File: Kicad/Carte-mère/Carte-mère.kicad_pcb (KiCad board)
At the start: 2 copper layers, 3 parts

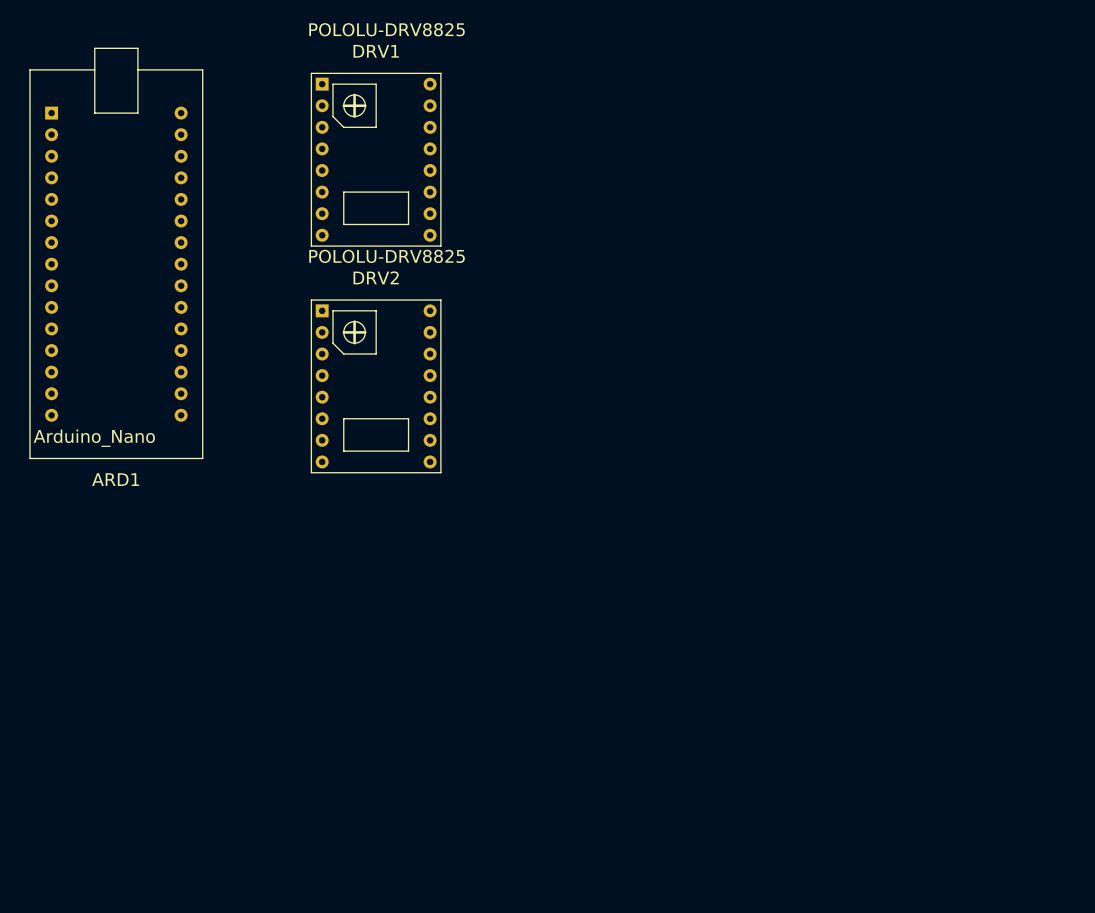
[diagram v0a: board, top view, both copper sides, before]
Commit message: Modification du circuit imprimée
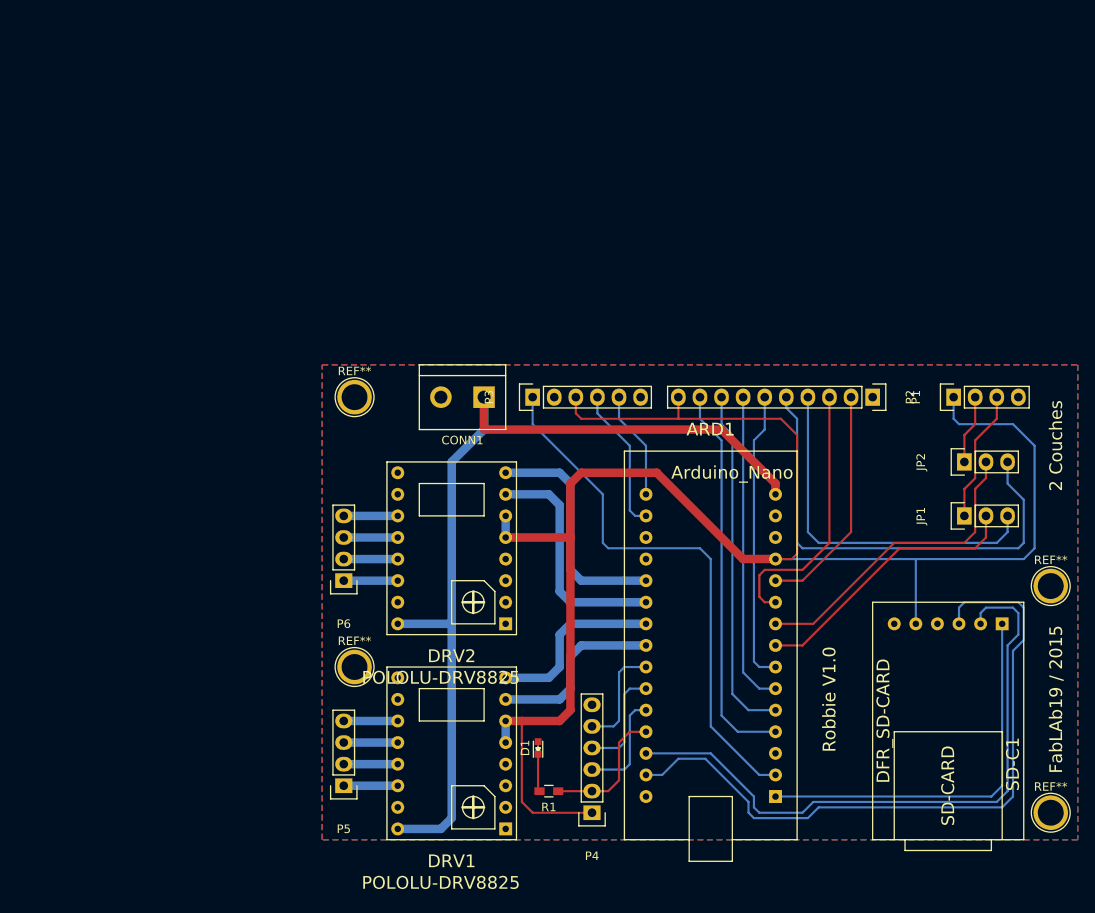
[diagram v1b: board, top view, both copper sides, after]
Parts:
- added CONN1: CONN_2, Connect:bornier2, F.Cu at (116.8, 86.4)
- added D1: LED, LEDs:LED-0603, F.Cu at (125.7, 127.6)
- added JP1: JUMPER3, Pin_Headers:Pin_Header_Straight_1x03, F.Cu at (175.9, 100.3)
- added JP2: JUMPER3, Pin_Headers:Pin_Header_Straight_1x03, F.Cu at (175.9, 94.0)
- added P1: CONN_01X10, Pin_Headers:Pin_Header_Straight_1x10, F.Cu at (165.1, 86.4)
- added P2: CONN_01X04, Pin_Headers:Pin_Header_Straight_1x04, F.Cu at (174.6, 86.4)
- added P3: CONN_01X06, Pin_Headers:Pin_Header_Straight_1x06, F.Cu at (125.1, 86.4)
- added P4: CONN_01X06, Pin_Headers:Pin_Header_Straight_1x06, F.Cu at (132.1, 135.3)
- added P5: CONN_01X04, Pin_Headers:Pin_Header_Straight_1x04, F.Cu at (102.9, 132.1)
- added P6: CONN_01X04, Pin_Headers:Pin_Header_Straight_1x04, F.Cu at (102.9, 108.0)
- added R1: 200, Resistors_SMD:R_0603_HandSoldering, F.Cu at (127.0, 132.7)
- added REF**: 1pin, Connect:1pin, F.Cu at (186.1, 135.3)
- added REF**: 1pin, Connect:1pin, F.Cu at (186.1, 108.6)
- added REF**: 1pin, Connect:1pin, F.Cu at (104.1, 86.4)
- added REF**: 1pin, Connect:1pin, F.Cu at (104.1, 118.1)
- added SD-C1: DFR_SD-CARD, DF-ROBOT_SD-CARD:DFR_SD-CARD, F.Cu at (172.7, 113.0)
- moved ARD1 85.9 mm to (146.1, 118.1), turned to 180 degrees
- moved DRV1 67.6 mm to (114.3, 127.0), turned to 180 degrees
- moved DRV2 17.7 mm to (114.3, 102.9), turned to 180 degrees
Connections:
- ARD1 pad 1: (no net) -> Net-(ARD1-Pad1)
- ARD1 pad 10: (no net) -> Net-(ARD1-Pad10)
- ARD1 pad 11: (no net) -> Net-(ARD1-Pad11)
- ARD1 pad 12: (no net) -> +5V
- ARD1 pad 14: (no net) -> GND
- ARD1 pad 15: (no net) -> +BATT
- ARD1 pad 16: (no net) -> Net-(ARD1-Pad16)
- ARD1 pad 17: (no net) -> Net-(ARD1-Pad17)
- ARD1 pad 2: (no net) -> +3.3V
- ARD1 pad 20: (no net) -> Net-(ARD1-Pad20)
- ARD1 pad 21: (no net) -> Net-(ARD1-Pad21)
- ARD1 pad 22: (no net) -> Net-(ARD1-Pad22)
- ARD1 pad 23: (no net) -> Net-(ARD1-Pad23)
- ARD1 pad 24: (no net) -> Net-(ARD1-Pad24)
- ARD1 pad 25: (no net) -> Net-(ARD1-Pad25)
- ARD1 pad 26: (no net) -> Net-(ARD1-Pad26)
- ARD1 pad 27: (no net) -> Net-(ARD1-Pad27)
- ARD1 pad 28: (no net) -> Net-(ARD1-Pad28)
- ARD1 pad 29: (no net) -> Net-(ARD1-Pad29)
- ARD1 pad 4: (no net) -> Net-(ARD1-Pad4)
- ARD1 pad 5: (no net) -> Net-(ARD1-Pad5)
- ARD1 pad 6: (no net) -> Net-(ARD1-Pad6)
- ARD1 pad 7: (no net) -> Net-(ARD1-Pad7)
- ARD1 pad 8: (no net) -> Net-(ARD1-Pad8)
- ARD1 pad 9: (no net) -> Net-(ARD1-Pad9)
- DRV1 pad 11: (no net) -> Net-(DRV1-Pad11)
- DRV1 pad 12: (no net) -> Net-(DRV1-Pad12)
- DRV1 pad 13: (no net) -> Net-(DRV1-Pad13)
- DRV1 pad 14: (no net) -> Net-(DRV1-Pad14)
- DRV1 pad 16: (no net) -> +BATT
- DRV1 pad 5: (no net) -> +5V
- DRV1 pad 6: (no net) -> +5V
- DRV1 pad 7: (no net) -> Net-(ARD1-Pad23)
- DRV1 pad 8: (no net) -> Net-(ARD1-Pad22)
- DRV1 pad 9: (no net) -> GND
- DRV2 pad 11: (no net) -> Net-(DRV2-Pad11)
- DRV2 pad 12: (no net) -> Net-(DRV2-Pad12)
- DRV2 pad 13: (no net) -> Net-(DRV2-Pad13)
- DRV2 pad 14: (no net) -> Net-(DRV2-Pad14)
- DRV2 pad 16: (no net) -> +BATT
- DRV2 pad 5: (no net) -> +5V
- DRV2 pad 6: (no net) -> +5V
- DRV2 pad 7: (no net) -> Net-(ARD1-Pad21)
- DRV2 pad 8: (no net) -> Net-(ARD1-Pad20)
- DRV2 pad 9: (no net) -> GND
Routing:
- net +5V: track 0.00 -> 207.1 mm
- net +BATT: track 0.00 -> 106.3 mm
- net Net-(ARD1-Pad29): track 0.00 -> 81.5 mm
- net Net-(ARD1-Pad28): track 0.00 -> 75.0 mm
- net +3.3V: track 0.00 -> 63.7 mm
- net Net-(JP2-Pad3): track 0.00 -> 55.2 mm
- net Net-(ARD1-Pad1): track 0.00 -> 46.2 mm
- net Net-(ARD1-Pad4): track 0.00 -> 45.7 mm
- net Net-(JP1-Pad3): track 0.00 -> 42.3 mm
- net Net-(ARD1-Pad5): track 0.00 -> 41.3 mm
- net Net-(ARD1-Pad6): track 0.00 -> 37.0 mm
- net Net-(ARD1-Pad9): track 0.00 -> 36.7 mm
- net Net-(ARD1-Pad7): track 0.00 -> 35.7 mm
- net Net-(ARD1-Pad8): track 0.00 -> 32.6 mm
- net Net-(ARD1-Pad10): track 0.00 -> 31.7 mm
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- added copper zone on B.Cu, net GND
- added copper zone on F.Cu, net GND
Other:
- net class 1mm added: clearance 0.254, trace_width 1, via_dia 1.635, via_drill 1
- net class 2mm added: clearance 0.254, trace_width 2, via_dia 2.635, via_drill 2
- rule pad_to_mask_clearance: 0 -> 0.2
- board text added: "2 Couches"
- board text added: "FabLAb19 / 2015"
- board text added: "Robbie V1.0"

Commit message: Mise à jour de la carte mère
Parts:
- removed the REF** at (186.1, 135.3)
- removed the REF** at (186.1, 108.6)
- removed the REF** at (104.1, 118.1)
- added REF**: 1pin, Connect:1pin, F.Cu at (104.1, 116.8)
- added REF**: 1pin, Connect:1pin, F.Cu at (185.4, 134.6)
- added REF**: 1pin, Connect:1pin, F.Cu at (185.4, 109.2)
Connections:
- ARD1 pad 19: (no net) -> GND
- DRV1 pad 15: (no net) -> GND
- DRV2 pad 15: (no net) -> GND
- REF** pad 1: (no net) -> GND
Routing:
- net +5V: track 207.1 -> 205.6 mm
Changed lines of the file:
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@@
 (kicad_pcb (version 4) (host pcbnew "(2014-jul-16 BZR unknown)-product")
   (general
-    (links 57)
-    (no_connects 1)
+    (links 62)
+    (no_connects 0)
     (area 0 0 0 0)
     (thickness 1.6)
     (drawings 7)
-    (tracks 211)
+    (tracks 213)
     (zones 0)
     (modules 19)
@@
     (mod_text_size 1.5 1.5)
     (mod_text_width 0.15)
-    (pad_size 1.524 1.524)
-    (pad_drill 0.762)
+    (pad_size 4.064 4.064)
+    (pad_drill 3.048)
     (pad_to_mask_clearance 0.2)
     (aux_axis_origin 0 0)
@@
       (net 15 "Net-(ARD1-Pad17)"))
     (pad 18 thru_hole circle (at 7.62 15.24 180) (size 1.524 1.524) (drill 0.762) (layers *.Cu *.Mask F.SilkS))
-    (pad 19 thru_hole circle (at 7.62 12.7 180) (size 1.524 1.524) (drill 0.762) (layers *.Cu *.Mask F.SilkS))
+    (pad 19 thru_hole circle (at 7.62 12.7 180) (size 1.524 1.524) (drill 0.762) (layers *.Cu *.Mask F.SilkS)
+      (net 12 GND))
     (pad 20 thru_hole circle (at 7.62 10.16 180) (size 1.524 1.524) (drill 0.762) (layers *.Cu *.Mask F.SilkS)
       (net 16 "Net-(ARD1-Pad20)"))
@@
     (pad 14 thru_hole circle (at 5.08 -5.08 180) (size 1.524 1.524) (drill 0.762) (layers *.Cu *.Mask F.SilkS)
       (net 30 "Net-(DRV1-Pad14)"))
-    (pad 15 thru_hole circle (at 5.08 -7.62 180) (size 1.524 1.524) (drill 0.762) (layers *.Cu *.Mask F.SilkS))
+    (pad 15 thru_hole circle (at 5.08 -7.62 180) (size 1.524 1.524) (drill 0.762) (layers *.Cu *.Mask F.SilkS)
+      (net 12 GND))
     (pad 16 thru_hole circle (at 5.08 -10.16 180) (size 1.524 1.524) (drill 0.762) (layers *.Cu *.Mask F.SilkS)
       (net 13 +BATT))
@@
     (pad 14 thru_hole circle (at 5.08 -5.08 180) (size 1.524 1.524) (drill 0.762) (layers *.Cu *.Mask F.SilkS)
       (net 34 "Net-(DRV2-Pad14)"))
-    (pad 15 thru_hole circle (at 5.08 -7.62 180) (size 1.524 1.524) (drill 0.762) (layers *.Cu *.Mask F.SilkS))
+    (pad 15 thru_hole circle (at 5.08 -7.62 180) (size 1.524 1.524) (drill 0.762) (layers *.Cu *.Mask F.SilkS)
+      (net 12 GND))
     (pad 16 thru_hole circle (at 5.08 -10.16 180) (size 1.524 1.524) (drill 0.762) (layers *.Cu *.Mask F.SilkS)
       (net 13 +BATT))
@@
   )
   (module Connect:1pin (layer F.Cu)
-    (at 186.055 135.255)
-    (descr "module 1 pin (ou trou mecanique de percage)")
-    (tags DEV)
-    (fp_text reference REF** (at 0 -3.048) (layer F.SilkS)
-      (effects (font (size 1 1) (thickness 0.15)))
-    )
-    (fp_text value 1pin (at 0 2.794) (layer F.Fab)
-      (effects (font (size 1 1) (thickness 0.15)))
-    )
-    (fp_circle (center 0 0) (end 0 -2.286) (layer F.SilkS) (width 0.15))
-    (pad 1 thru_hole circle (at 0 0) (size 4.064 4.064) (drill 3.048) (layers *.Cu *.Mask F.SilkS))
-  )
-  (module Connect:1pin (layer F.Cu)
-    (at 186.055 108.585)
-    (descr "module 1 pin (ou trou mecanique de percage)")
-    (tags DEV)
-    (fp_text reference REF** (at 0 -3.048) (layer F.SilkS)
-      (effects (font (size 1 1) (thickness 0.15)))
-    )
-    (fp_text value 1pin (at 0 2.794) (layer F.Fab)
-      (effects (font (size 1 1) (thickness 0.15)))
-    )
-    (fp_circle (center 0 0) (end 0 -2.286) (layer F.SilkS) (width 0.15))
-    (pad 1 thru_hole circle (at 0 0) (size 4.064 4.064) (drill 3.048) (layers *.Cu *.Mask F.SilkS))
-  )
-  (module Connect:1pin (layer F.Cu)
     (at 104.14 86.36)
     (descr "module 1 pin (ou trou mecanique de percage)")
@@
     )
     (fp_circle (center 0 0) (end 0 -2.286) (layer F.SilkS) (width 0.15))
-    (pad 1 thru_hole circle (at 0 0) (size 4.064 4.064) (drill 3.048) (layers *.Cu *.Mask F.SilkS))
+    (pad 1 thru_hole circle (at 0 0) (size 4.064 4.064) (drill 3.048) (layers *.Cu *.Mask F.SilkS)
+      (net 12 GND))
   )
   (module Connect:1pin (layer F.Cu)
-    (at 104.14 118.11)
+    (at 104.14 116.84)
     (descr "module 1 pin (ou trou mecanique de percage)")
     (tags DEV)
@@
     )
     (fp_circle (center 0 0) (end 0 -2.286) (layer F.SilkS) (width 0.15))
-    (pad 1 thru_hole circle (at 0 0) (size 4.064 4.064) (drill 3.048) (layers *.Cu *.Mask F.SilkS))
+    (pad GND thru_hole circle (at 0 0) (size 4.064 4.064) (drill 3.048) (layers *.Cu *.Mask F.SilkS))
+  )
+  (module Connect:1pin (layer F.Cu)
+    (at 185.42 134.62)
+    (descr "module 1 pin (ou trou mecanique de percage)")
+    (tags DEV)
+    (fp_text reference REF** (at 0 -3.048) (layer F.SilkS)
+      (effects (font (size 1 1) (thickness 0.15)))
+    )
+    (fp_text value 1pin (at 0 2.794) (layer F.Fab)
+      (effects (font (size 1 1) (thickness 0.15)))
+    )
+    (fp_circle (center 0 0) (end 0 -2.286) (layer F.SilkS) (width 0.15))
+    (pad GND thru_hole circle (at 0 0) (size 4.064 4.064) (drill 3.048) (layers *.Cu *.Mask F.SilkS))
+  )
+  (module Connect:1pin (layer F.Cu)
+    (at 185.42 109.22)
+    (descr "module 1 pin (ou trou mecanique de percage)")
+    (tags DEV)
+    (fp_text reference REF** (at 0 -3.048) (layer F.SilkS)
+      (effects (font (size 1 1) (thickness 0.15)))
+    )
+    (fp_text value 1pin (at 0 2.794) (layer F.Fab)
+      (effects (font (size 1 1) (thickness 0.15)))
+    )
+    (fp_circle (center 0 0) (end 0 -2.286) (layer F.SilkS) (width 0.15))
+    (pad 1 thru_hole circle (at 0 0) (size 4.064 4.064) (drill 3.048) (layers *.Cu *.Mask F.SilkS)
+      (net 12 GND))
   )
   (gr_text "2 Couches" (at 186.69 92.075 90) (layer F.SilkS)
@@
   (segment (start 179.07 133.35) (end 153.67 133.35) (width 0.254) (layer B.Cu) (net 1))
   (segment (start 180.34 132.08) (end 179.07 133.35) (width 0.254) (layer B.Cu) (net 1))
-  (segment (start 125.095 86.36) (end 125.095 89.535) (width 0.254) (layer B.Cu) (net 2))
+  (segment (start 125.095 86.36) (end 125.095 88.9) (width 0.254) (layer B.Cu) (net 2) (status 400000))
   (segment (start 151.765 130.81) (end 153.67 130.81) (width 0.254) (layer B.Cu) (net 2))
   (segment (start 146.05 125.095) (end 151.765 130.81) (width 0.254) (layer B.Cu) (net 2))
@@
   (segment (start 133.985 104.14) (end 144.78 104.14) (width 0.254) (layer B.Cu) (net 2))
   (segment (start 133.35 103.505) (end 133.985 104.14) (width 0.254) (layer B.Cu) (net 2))
-  (segment (start 133.35 97.79) (end 133.35 103.505) (width 0.254) (layer B.Cu) (net 2))
-  (segment (start 125.095 89.535) (end 133.35 97.79) (width 0.254) (layer B.Cu) (net 2))
+  (segment (start 133.35 97.155) (end 133.35 103.505) (width 0.254) (layer B.Cu) (net 2))
+  (segment (start 125.095 88.9) (end 133.35 97.155) (width 0.254) (layer B.Cu) (net 2))
   (segment (start 144.78 86.36) (end 144.78 88.9) (width 0.254) (layer B.Cu) (net 3))
   (segment (start 149.225 125.73) (end 153.67 125.73) (width 0.254) (layer B.Cu) (net 3))
@@
   (segment (start 125.095 135.255) (end 132.08 135.255) (width 0.254) (layer F.Cu) (net 11))
   (segment (start 123.825 133.985) (end 125.095 135.255) (width 0.254) (layer F.Cu) (net 11))
-  (segment (start 129.54 102.87) (end 129.54 123.19) (width 1) (layer F.Cu) (net 11))
-  (segment (start 128.27 124.46) (end 123.825 124.46) (width 1) (layer F.Cu) (net 11))
   (segment (start 123.825 124.46) (end 121.92 124.46) (width 1) (layer F.Cu) (net 11))
-  (segment (start 129.54 123.19) (end 128.27 124.46) (width 1) (layer F.Cu) (net 11))
   (segment (start 121.92 102.87) (end 129.54 102.87) (width 1) (layer F.Cu) (net 11))
+  (segment (start 130.81 95.25) (end 139.7 95.25) (width 1) (layer F.Cu) (net 11))
+  (segment (start 129.54 96.52) (end 130.81 95.25) (width 1) (layer F.Cu) (net 11))
+  (segment (start 129.54 102.87) (end 129.54 96.52) (width 1) (layer F.Cu) (net 11))
   (segment (start 149.86 105.41) (end 153.67 105.41) (width 1) (layer F.Cu) (net 11))
-  (segment (start 129.54 102.87) (end 129.54 96.52) (width 1) (layer F.Cu) (net 11))
-  (segment (start 129.54 96.52) (end 130.81 95.25) (width 1) (layer F.Cu) (net 11))
-  (segment (start 130.81 95.25) (end 139.7 95.25) (width 1) (layer F.Cu) (net 11))
   (segment (start 139.7 95.25) (end 149.86 105.41) (width 1) (layer F.Cu) (net 11))
   (segment (start 121.92 124.46) (end 121.92 127) (width 1) (layer B.Cu) (net 11))
   (segment (start 121.92 100.33) (end 121.92 102.87) (width 1) (layer B.Cu) (net 11))
+  (segment (start 125.73 124.46) (end 127 123.19) (width 1) (layer F.Cu) (net 11))
+  (segment (start 127 123.19) (end 127 108.585) (width 1) (layer F.Cu) (net 11))
+  (segment (start 127 108.585) (end 129.54 106.045) (width 1) (layer F.Cu) (net 11))
+  (segment (start 129.54 106.045) (end 129.54 102.87) (width 1) (layer F.Cu) (net 11))
+  (segment (start 123.825 124.46) (end 125.73 124.46) (width 1) (layer F.Cu) (net 11))
   (segment (start 119.38 86.36) (end 119.38 90.17) (width 1) (layer F.Cu) (net 13))
   (segment (start 153.67 96.52) (end 153.67 97.79) (width 1) (layer F.Cu) (net 13))

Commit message: Modification PCB pour prendre en compte les remarques faites à l'IUT
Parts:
- removed the REF** at (104.1, 86.4)
- removed the REF** at (104.1, 116.8)
- removed the REF** at (185.4, 134.6)
- removed the REF** at (185.4, 109.2)
- added BPN1: Bouton_poussoir_CI, Boutons:BPN-CI, F.Cu at (189.9, 128.3)
- added P7: CONN_01X02, Pin_Headers:Pin_Header_Straight_1x02, F.Cu at (168.3, 96.5)
- added REF**: 1pin, Connect:1pin, F.Cu at (191.1, 147.3)
- added REF**: 1pin, Connect:1pin, F.Cu at (109.9, 147.3)
- added REF**: 1pin, Connect:1pin, F.Cu at (109.9, 68.6)
- added REF**: 1pin, Connect:1pin, F.Cu at (191.1, 68.6)
- moved R1 69.5 mm to (191.1, 106.0), turned to 270 degrees
- moved D1 67.3 mm to (191.1, 111.8), turned to 270 degrees
- moved P4 45.3 mm to (155.6, 96.5), turned to 270 degrees
- moved P3 33.0 mm to (155.6, 73.7), turned to 270 degrees
- moved P1 22.4 mm to (183.5, 73.7)
- moved JP2 18.0 mm to (173.4, 111.8), turned to 180 degrees
- moved DRV1 14.8 mm to (125.1, 137.2)
- moved ARD1 14.7 mm to (150.5, 132.1)
- moved DRV2 14.0 mm to (125.1, 111.8)
- moved SD-C1 14.0 mm to (173.4, 127.0)
- moved P2 13.5 mm to (183.5, 96.5), turned to 270 degrees
- moved JP1 11.7 mm to (178.4, 111.8), turned to 180 degrees
- moved P5 10.8 mm to (112.4, 137.2)
- moved P6 10.3 mm to (112.4, 111.8)
- moved CONN1 3.18 mm to (114.9, 88.9), turned to 270 degrees
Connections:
- ARD1 pad 13: (no net) -> Net-(ARD1-Pad13)
- ARD1 pad 18: (no net) -> Net-(ARD1-Pad18)
- ARD1 pad 30: (no net) -> Net-(ARD1-Pad30)
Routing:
- net (no net): track 0.00 -> 362.2 mm
- net Net-(ARD1-Pad27): track 15.8 -> 168.2 mm
- net +BATT: track 106.3 -> 223.1 mm
- net Net-(ARD1-Pad13): track 0.00 -> 62.7 mm
- net Net-(ARD1-Pad18): track 0.00 -> 58.7 mm
- net Net-(ARD1-Pad30): track 0.00 -> 58.5 mm
- net +5V: track 205.6 -> 259.7 mm
- net Net-(ARD1-Pad11): track 27.1 -> 72.8 mm
- net Net-(ARD1-Pad10): track 31.7 -> 76.0 mm
- net +3.3V: track 63.7 -> 99.2 mm
- net Net-(ARD1-Pad26): track 12.6 -> 47.3 mm
- net Net-(ARD1-Pad6): track 37.0 -> 71.3 mm
- net Net-(ARD1-Pad17): track 17.1 -> 50.9 mm
- net Net-(ARD1-Pad5): track 41.3 -> 74.6 mm
- net Net-(ARD1-Pad16): track 12.7 -> 46.0 mm
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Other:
- net class 0.5mm added: clearance 0.254, trace_width 0.5, via_dia 1.135, via_drill 0.6

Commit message: Ajout de la refonte de la carte mère
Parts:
- removed JP1, JP2: JUMPER3, Pin_Headers:Pin_Header_Straight_1x03
- removed the REF** at (191.1, 147.3)
- removed the REF** at (109.9, 147.3)
- removed the REF** at (109.9, 68.6)
- removed the REF** at (191.1, 68.6)
- added REF**: 1pin, Connect:1pin, F.Cu at (109.2, 68.6)
- added REF**: Pin_Header_Straight_1x10, Pin_Headers:Pin_Header_Straight_1x10, F.Cu at (116.8, 78.7)
- added REF**: Pin_Header_Straight_1x10, Pin_Headers:Pin_Header_Straight_1x10, F.Cu at (116.8, 81.3)
- added REF**: 1pin, Connect:1pin, F.Cu at (190.5, 68.6)
- added REF**: 1pin, Connect:1pin, F.Cu at (190.5, 147.3)
- added REF**: 1pin, Connect:1pin, F.Cu at (109.2, 147.3)
- added REF**: Pin_Header_Straight_1x10, Pin_Headers:Pin_Header_Straight_1x10, F.Cu at (116.8, 66.0)
- added REF**: Pin_Header_Straight_1x10, Pin_Headers:Pin_Header_Straight_1x10, F.Cu at (116.8, 68.6)
- added REF**: Pin_Header_Straight_1x10, Pin_Headers:Pin_Header_Straight_1x10, F.Cu at (116.8, 71.1)
- added REF**: Pin_Header_Straight_1x10, Pin_Headers:Pin_Header_Straight_1x10, F.Cu at (116.8, 73.7)
- added REF**: Pin_Header_Straight_1x10, Pin_Headers:Pin_Header_Straight_1x10, F.Cu at (116.8, 76.2)
- P1: value CONN_01X10 -> CONN_01X08; footprint Pin_Headers:Pin_Header_Straight_1x10 -> Pin_Headers:Pin_Header_Straight_1x08
- moved D1 52.3 mm to (143.5, 90.2), turned to 180 degrees
- moved R1 45.4 mm to (148.6, 90.2), turned to 180 degrees
- moved P7 21.1 mm to (189.2, 94.0)
- moved BPN1 15.6 mm to (182.9, 114.3)
- moved CONN1 8.25 mm to (111.8, 96.5)
- moved P1 5.12 mm to (188.0, 76.2)
- moved P3 5.12 mm to (160.0, 76.2)
- moved P4 5.12 mm to (160.0, 94.0)
- moved P6 5.12 mm to (111.8, 116.8)
- moved P2 3.17 mm to (181.6, 94.0)
- moved SD-C1 1.91 mm to (175.3, 127.0)
- moved P5 0.63 mm to (111.8, 137.2)
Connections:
- ARD1 pad 18: Net-(ARD1-Pad18) -> (no net)
- P1 pad 4: Net-(JP1-Pad3) -> Net-(ARD1-Pad7)
- P1 pad 5: Net-(JP2-Pad3) -> Net-(ARD1-Pad6)
- P1 pad 6: Net-(ARD1-Pad7) -> Net-(ARD1-Pad5)
- P1 pad 7: Net-(ARD1-Pad6) -> Net-(ARD1-Pad4)
- P1 pad 8: Net-(ARD1-Pad5) -> +5V
- P2 pad 2: Net-(JP2-Pad1) -> Net-(ARD1-Pad9)
- P2 pad 3: Net-(JP1-Pad1) -> Net-(ARD1-Pad8)
- P3 pad 2: (no net) -> GND
- P7 pad 1: Net-(ARD1-Pad18) -> Net-(ARD1-Pad13)
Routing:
- net +BATT: track 223.1 -> 115.2 mm
- net Net-(ARD1-Pad27): track 168.2 -> 67.5 mm
- net Net-(ARD1-Pad18): track 58.7 -> 0.00 mm
- net Net-(JP2-Pad3): track 44.4 -> 0.00 mm
- net +3.3V: track 99.2 -> 141.5 mm
- net Net-(JP1-Pad3): track 38.7 -> 0.00 mm
- net Net-(JP2-Pad1): track 29.9 -> 0.00 mm
- net Net-(ARD1-Pad9): track 31.9 -> 59.2 mm
- net +5V: track 259.7 -> 283.2 mm
- net Net-(ARD1-Pad8): track 37.7 -> 57.5 mm
- net Net-(JP1-Pad1): track 19.4 -> 0.00 mm
- net Net-(ARD1-Pad29): track 60.0 -> 79.1 mm
- net Net-(ARD1-Pad17): track 50.9 -> 65.5 mm
- net Net-(ARD1-Pad7): track 68.0 -> 80.3 mm
- net Net-(ARD1-Pad11): track 72.8 -> 84.5 mm
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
